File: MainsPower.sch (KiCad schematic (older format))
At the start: 17 parts

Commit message: Few minor changes
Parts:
- removed F?: 12A, symbol Device:Fuse
- added F?: 12A, symbol Device:Fuse
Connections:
- net LN_NEUTRAL_OUT: now also K?.4 (NO), K?.5 (NO)
- net VACN: now also F?.1; no longer F?.2, K?.3 (COM), K?.6 (COM)
- new net: F?.2, K?.3 (COM), K?.6 (COM)
- new net VACL: F?.2
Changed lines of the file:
@@
 Wire Notes Line
 	3200 2650 3200 950
-Text Notes 3900 950  2    50   ~ 0
+Text Notes 3900 900  2    50   ~ 0
 AC/DC Conversion
 Wire Wire Line
@@
 	3900 1600 4450 1600
 Text Label 3250 1600 0    50   ~ 0
-VACN
+VACL
 Wire Notes Line
 	3200 2650 6300 2650
@@
 U 1 1 5F6C751D
 P 2750 4500
-F 0 "U?" H 2750 5415 50  0000 C CNN
-F 1 "MAX4684_5" H 2750 5324 50  0000 C CNN
+F 0 "U?" H 2350 5300 50  0000 C CNN
+F 1 "MAX4684_5" H 3000 5300 50  0000 C CNN
 F 2 "" H 2550 5050 50  0001 C CNN
 F 3 "" H 2550 5050 50  0001 C CNN
@@
 Wire Wire Line
 	5300 4550 5200 4550
-Wire Wire Line
-	5300 4550 6150 4550
-Connection ~ 5300 4550
 Text Label 6150 4550 2    50   ~ 0
 VACN
@@
 Text Notes 1600 2800 2    50   ~ 0
 Output Relay Switching
-$Comp
-L Device:Fuse F?
-U 1 1 5F74E046
-P 5300 3900
-F 0 "F?" V 5103 3900 50  0000 C CNN
-F 1 "12A" V 5194 3900 50  0000 C CNN
-F 2 "" V 5230 3900 50  0001 C CNN
-F 3 "~" H 5300 3900 50  0001 C CNN
-	1    5300 3900
-	0    1    1    0
-$EndComp
-Wire Wire Line
-	4950 3900 5150 3900
 Connection ~ 4950 3900
 Text Label 6150 3900 2    50   ~ 0
 LN_NEUTRAL_OUT
-Wire Wire Line
-	5450 3900 6150 3900
 NoConn ~ 5650 2000
+$Comp
+L Device:Fuse F?
+U 1 1 5F75BE1A
+P 5650 4550
+F 0 "F?" V 5453 4550 50  0000 C CNN
+F 1 "12A" V 5544 4550 50  0000 C CNN
+F 2 "" V 5580 4550 50  0001 C CNN
+F 3 "~" H 5650 4550 50  0001 C CNN
+	1    5650 4550
+	0    1    1    0
+$EndComp
+Wire Wire Line
+	5300 4550 5500 4550
+Connection ~ 5300 4550
+Wire Wire Line
+	5800 4550 6150 4550
+Wire Wire Line
+	4950 3900 6150 3900
 $EndSCHEMATC

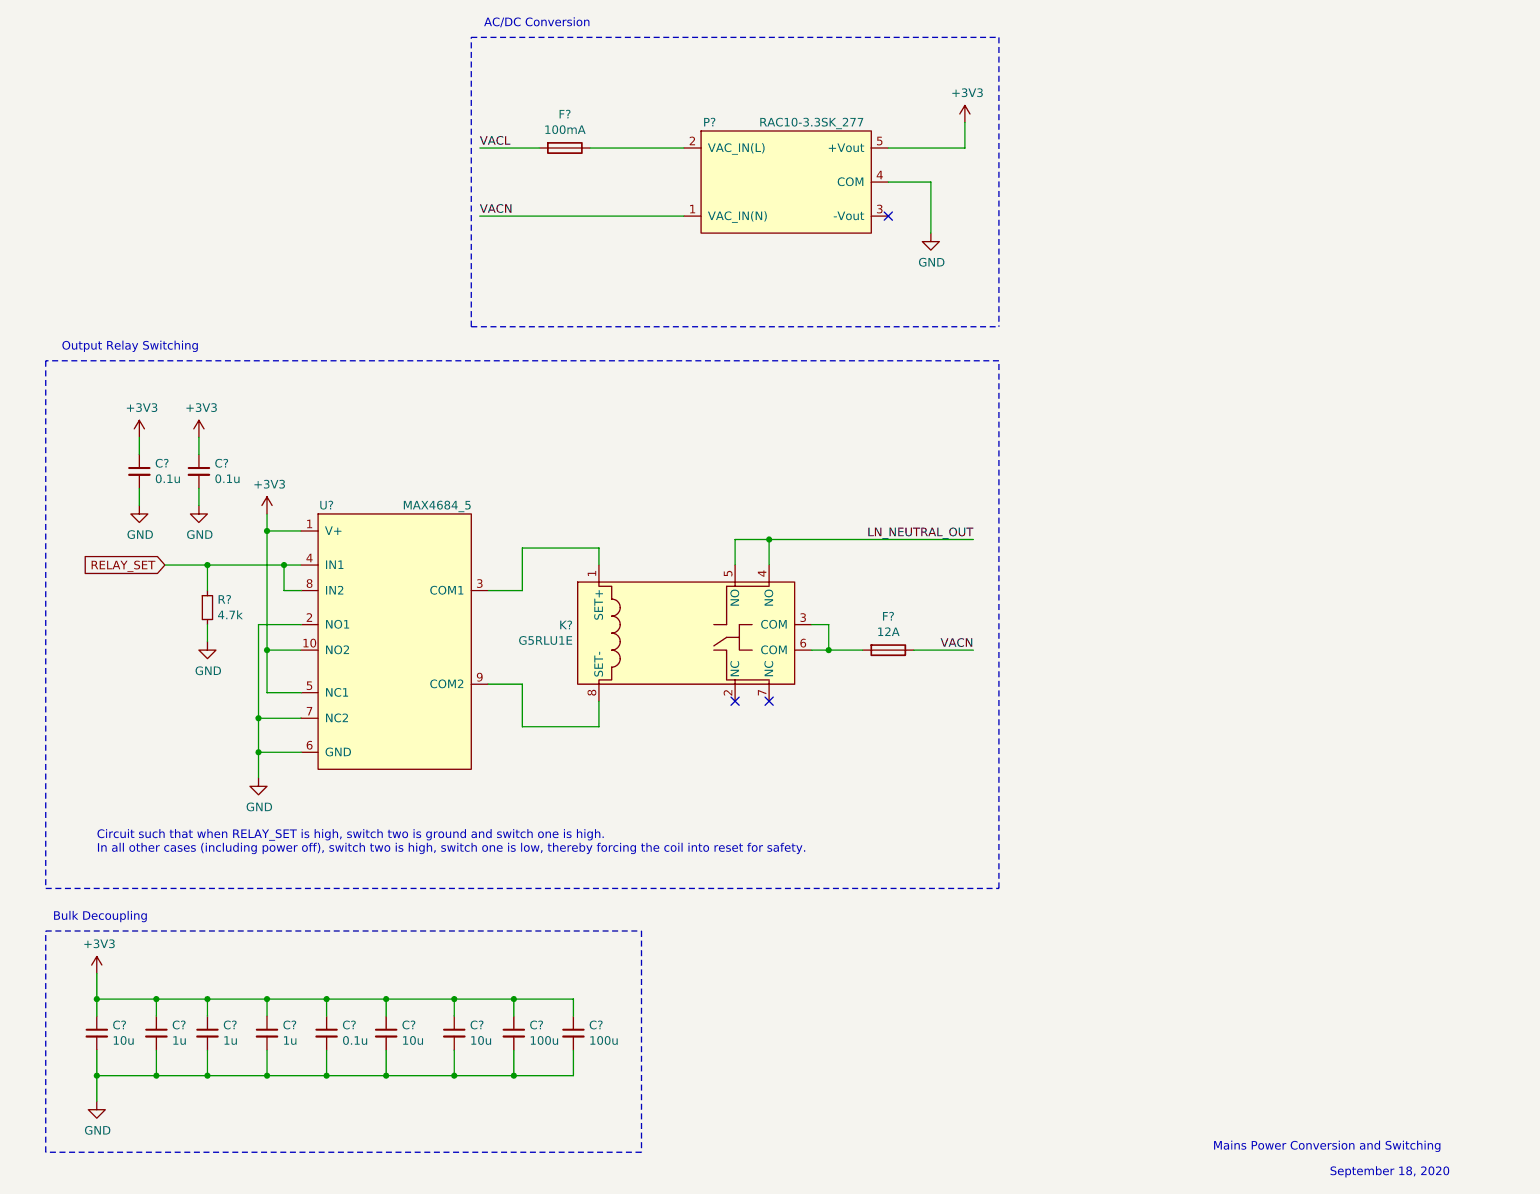
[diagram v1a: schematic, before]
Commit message: Added connectors
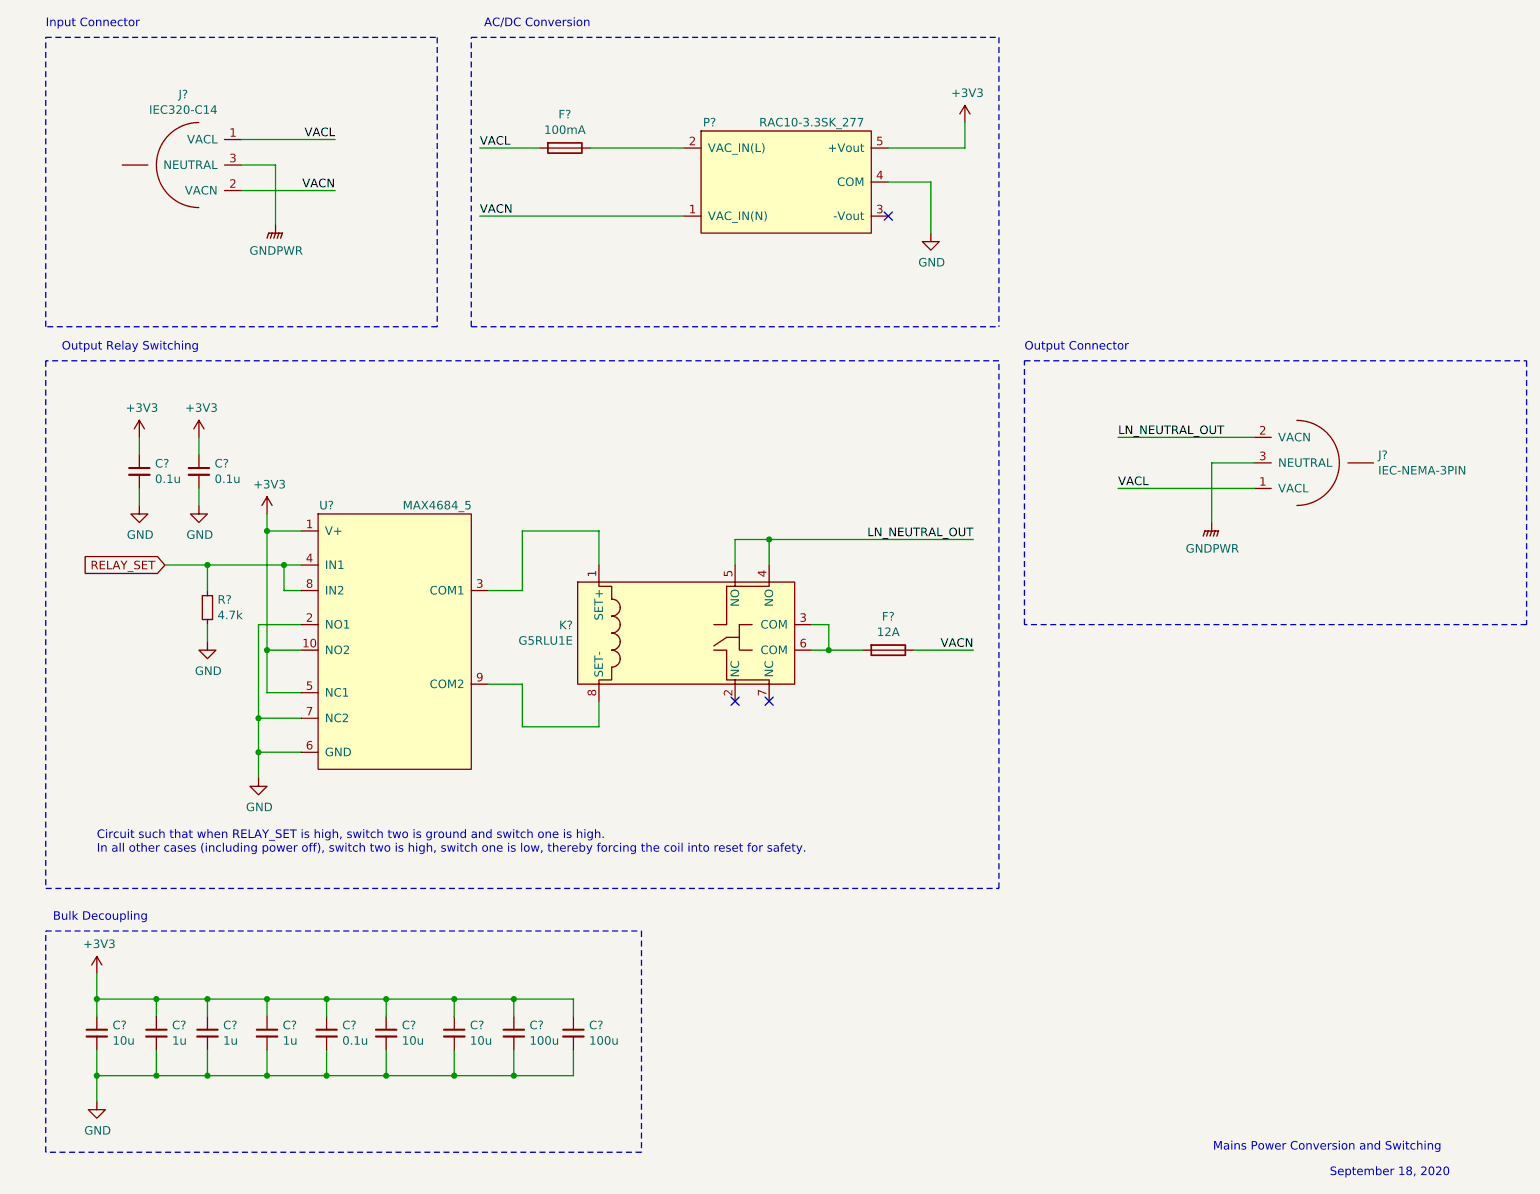
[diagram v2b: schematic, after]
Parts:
- added J?: IEC-NEMA-3PIN, symbol ReflowOven:IEC-NEMA-3PIN
- added J?: IEC320-C14, symbol ReflowOven:IEC320-C14
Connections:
- net LN_NEUTRAL_OUT: now also J?.2 (VACN)
- net VACL: now also J?.1 (VACL), J?.1 (VACL)
- net VACN: now also J?.2 (VACN)
- new net GNDPWR: J?.3 (NEUTRAL), J?.3 (NEUTRAL)
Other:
- note added: "Input Connector"
- note added: "Output Connector"
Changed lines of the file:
@@
 $EndComp
 $Comp
-L power:+3V3 #PWR?
+L power:+3V3 #PWR0101
 U 1 1 5F650E9B
 P 6100 1450
-F 0 "#PWR?" H 6100 1300 50  0001 C CNN
+F 0 "#PWR0101" H 6100 1300 50  0001 C CNN
 F 1 "+3V3" H 6115 1623 50  0000 C CNN
 F 2 "" H 6100 1450 50  0001 C CNN
@@
 	5650 1800 5900 1800
 $Comp
-L power:GND #PWR?
+L power:GND #PWR0102
 U 1 1 5F651956
 P 5900 2100
-F 0 "#PWR?" H 5900 1850 50  0001 C CNN
+F 0 "#PWR0102" H 5900 1850 50  0001 C CNN
 F 1 "GND" H 5905 1927 50  0000 C CNN
 F 2 "" H 5900 2100 50  0001 C CNN
@@
 	2350 6600 2700 6600
 $Comp
-L power:+3V3 #PWR?
+L power:+3V3 #PWR0103
 U 1 1 5F6552EA
 P 1000 6450
-F 0 "#PWR?" H 1000 6300 50  0001 C CNN
+F 0 "#PWR0103" H 1000 6300 50  0001 C CNN
 F 1 "+3V3" H 1015 6623 50  0000 C CNN
 F 2 "" H 1000 6450 50  0001 C CNN
@@
 	2350 7050 2700 7050
 $Comp
-L power:GND #PWR?
+L power:GND #PWR0104
 U 1 1 5F656CFD
 P 1000 7200
-F 0 "#PWR?" H 1000 6950 50  0001 C CNN
+F 0 "#PWR0104" H 1000 6950 50  0001 C CNN
 F 1 "GND" H 1005 7027 50  0000 C CNN
 F 2 "" H 1000 7200 50  0001 C CNN
@@
 	3300 4200 3500 4200
 Wire Wire Line
-	3500 4200 3500 3950
-Wire Wire Line
-	3500 3950 3950 3950
-Wire Wire Line
-	3950 3950 3950 4050
+	3500 4200 3500 3850
+Wire Wire Line
+	3500 3850 3950 3850
+Wire Wire Line
+	3950 3850 3950 4050
 Wire Wire Line
 	3950 5000 3500 5000
@@
 	1950 5150 2200 5150
 $Comp
-L power:GND #PWR?
+L power:GND #PWR0105
 U 1 1 5F6CEEB0
 P 1950 5300
-F 0 "#PWR?" H 1950 5050 50  0001 C CNN
+F 0 "#PWR0105" H 1950 5050 50  0001 C CNN
 F 1 "GND" H 1955 5127 50  0000 C CNN
 F 2 "" H 1950 5300 50  0001 C CNN
@@
 	2000 3850 2000 3750
 $Comp
-L power:+3V3 #PWR?
+L power:+3V3 #PWR0106
 U 1 1 5F6D2225
 P 2000 3750
-F 0 "#PWR?" H 2000 3600 50  0001 C CNN
+F 0 "#PWR0106" H 2000 3600 50  0001 C CNN
 F 1 "+3V3" H 2015 3923 50  0000 C CNN
 F 2 "" H 2000 3750 50  0001 C CNN
@@
 	1600 3600 1600 3700
 $Comp
-L power:GND #PWR?
+L power:GND #PWR0107
 U 1 1 5F6E6FE7
 P 1600 3700
-F 0 "#PWR?" H 1600 3450 50  0001 C CNN
+F 0 "#PWR0107" H 1600 3450 50  0001 C CNN
 F 1 "GND" H 1605 3527 50  0000 C CNN
 F 2 "" H 1600 3700 50  0001 C CNN
@@
 $EndComp
 $Comp
-L power:GND #PWR?
+L power:GND #PWR0108
 U 1 1 5F6E743A
 P 1250 3700
-F 0 "#PWR?" H 1250 3450 50  0001 C CNN
+F 0 "#PWR0108" H 1250 3450 50  0001 C CNN
 F 1 "GND" H 1255 3527 50  0000 C CNN
 F 2 "" H 1250 3700 50  0001 C CNN
@@
 	1250 3400 1250 3300
 $Comp
-L power:+3V3 #PWR?
+L power:+3V3 #PWR0109
 U 1 1 5F6EB717
 P 1600 3300
-F 0 "#PWR?" H 1600 3150 50  0001 C CNN
+F 0 "#PWR0109" H 1600 3150 50  0001 C CNN
 F 1 "+3V3" H 1615 3473 50  0000 C CNN
 F 2 "" H 1600 3300 50  0001 C CNN
@@
 $EndComp
 $Comp
-L power:+3V3 #PWR?
+L power:+3V3 #PWR0110
 U 1 1 5F6EBBB8
 P 1250 3300
-F 0 "#PWR?" H 1250 3150 50  0001 C CNN
+F 0 "#PWR0110" H 1250 3150 50  0001 C CNN
 F 1 "+3V3" H 1265 3473 50  0000 C CNN
 F 2 "" H 1250 3300 50  0001 C CNN
@@
 	1650 4400 1650 4500
 $Comp
-L power:GND #PWR?
+L power:GND #PWR0111
 U 1 1 5F707EBB
 P 1650 4500
-F 0 "#PWR?" H 1650 4250 50  0001 C CNN
+F 0 "#PWR0111" H 1650 4250 50  0001 C CNN
 F 1 "GND" H 1655 4327 50  0000 C CNN
 F 2 "" H 1650 4500 50  0001 C CNN
@@
 Wire Wire Line
 	4950 3900 6150 3900
+$Comp
+L ReflowOven:IEC-NEMA-3PIN J?
+U 1 1 5F769735
+P 8000 3450
+F 0 "J?" H 8528 3496 50  0000 L CNN
+F 1 "IEC-NEMA-3PIN" H 8528 3405 50  0000 L CNN
+F 2 "" H 7900 3375 50  0001 C CNN
+F 3 "" H 7900 3375 50  0001 C CNN
+	1    8000 3450
+	1    0    0    -1
+$EndComp
+Wire Wire Line
+	7800 3300 7000 3300
+Text Label 7000 3300 0    50   ~ 0
+LN_NEUTRAL_OUT
+Wire Wire Line
+	7800 3600 7000 3600
+Wire Wire Line
+	7800 3450 7550 3450
+Wire Wire Line
+	7550 3450 7550 3800
+$Comp
+L power:GNDPWR #PWR?
+U 1 1 5F7765D1
+P 7550 3800
+F 0 "#PWR?" H 7550 3600 50  0001 C CNN
+F 1 "GNDPWR" H 7554 3646 50  0000 C CNN
+F 2 "" H 7550 3750 50  0001 C CNN
+F 3 "" H 7550 3750 50  0001 C CNN
+	1    7550 3800
+	1    0    0    -1
+$EndComp
+Text Label 7000 3600 0    50   ~ 0
+VACL
+$Comp
+L ReflowOven:IEC320-C14 J?
+U 1 1 5F784C5C
+P 1650 1700
+F 0 "J?" H 1792 1285 50  0000 C CNN
+F 1 "IEC320-C14" H 1792 1376 50  0000 C CNN
+F 2 "" H 1550 1625 50  0001 C CNN
+F 3 "" H 1550 1625 50  0001 C CNN
+	1    1650 1700
+	-1   0    0    1
+$EndComp
+Wire Wire Line
+	1850 1700 2050 1700
+Wire Wire Line
+	2050 1700 2050 2050
+$Comp
+L power:GNDPWR #PWR?
+U 1 1 5F787509
+P 2050 2050
+F 0 "#PWR?" H 2050 1850 50  0001 C CNN
+F 1 "GNDPWR" H 2054 1896 50  0000 C CNN
+F 2 "" H 2050 2000 50  0001 C CNN
+F 3 "" H 2050 2000 50  0001 C CNN
+	1    2050 2050
+	1    0    0    -1
+$EndComp
+Wire Wire Line
+	1850 1850 2400 1850
+Wire Wire Line
+	1850 1550 2400 1550
+Text Label 2400 1550 2    50   ~ 0
+VACL
+Text Label 2400 1850 2    50   ~ 0
+VACN
+Wire Notes Line
+	3000 950  3000 2650
+Wire Notes Line
+	3000 2650 700  2650
+Wire Notes Line
+	700  2650 700  950
+Wire Notes Line
+	700  950  3000 950
+Text Notes 700  900  0    50   ~ 0
+Input Connector
+Wire Notes Line
+	6450 2850 9400 2850
+Wire Notes Line
+	9400 2850 9400 4400
+Wire Notes Line
+	9400 4400 6450 4400
+Wire Notes Line
+	6450 4400 6450 2850
+Text Notes 6450 2800 0    50   ~ 0
+Output Connector
 $EndSCHEMATC
